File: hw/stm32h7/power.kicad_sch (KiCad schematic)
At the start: 40 parts, among them J5 436500212, U4 LMR50410, U5 INA241A3xDDF, U6 TPS2116DRL, U7 TLV75733PDRV, U8 TLV75733PDRV

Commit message: WIP: H7 dual-axis encoder ports, VSENSE, LED swap, TPS2553/ESD on J4
- driver sheet: respaced; DRV8316C 3x-PWM pinout; J4 encoder port with
  100R series, 2.2k/5.1k pull-ups, TPD4E05U06 ESD array, TPS2553 current
  limited 5V switch (ENC_EN/ENC_SW_nFLT); phase VSENSE dividers
  (100k/8.2k, 8.2p/100p compensated); R55/R58/R62 footprint -> R_0201
- root sheet: second driver instance (driver2) for the dual-axis plan
- micro sheet: D1/D2 -> WS2812B-2020-V6 (3.3V logic), 5V0 feed
- power sheet: drop 3V3_VSENSE_AI (VREFINT instead), LMR50410 cleanup
- stm32h7.ioc: TIM1/TIM8 PWM, SPI2/SPI3/SPI4, TIM4 encoder, FDCAN1/2,
  QUADSPI bank 2
- datasheets: WS2812B-2020-V6, SK6805-EC15, TPS2553
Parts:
- removed C39: 0.1uF, Capacitor_SMD:C_0201_0603Metric, symbol Device:C_Small
- removed R21, R22: 5.1k, Resistor_SMD:R_0201_0603Metric, symbol Device:R_Small
- renumbered C30 to C32, C31 to C33, C32 to C34, C33 to C35, C34 to C36, C35 to C37, C36 to C38, C37 to C39, C38 to C40, C40 to C42, C41 to C43, R10 to R18, R11 to R19, R12 to R20, R13 to R21, R14 to R22, R15 to R23, R16 to R24, R17 to R25, R18 to R26, R19 to R27, R20 to R28, TP9 to TP10, TP3 to TP4, TP4 to TP5, TP5 to TP6, TP6 to TP7, TP7 to TP8, TP8 to TP9, U4 to U5, U5 to U6, U6 to U7, U7 to U8, U8 to U9
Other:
- moved on the sheet: D3, R28

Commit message: WIP: schematic bringup
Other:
- moved on the sheet: C32, C34, C36, C37, L1, R18, R19, R22, R23, R24, R25, TP4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

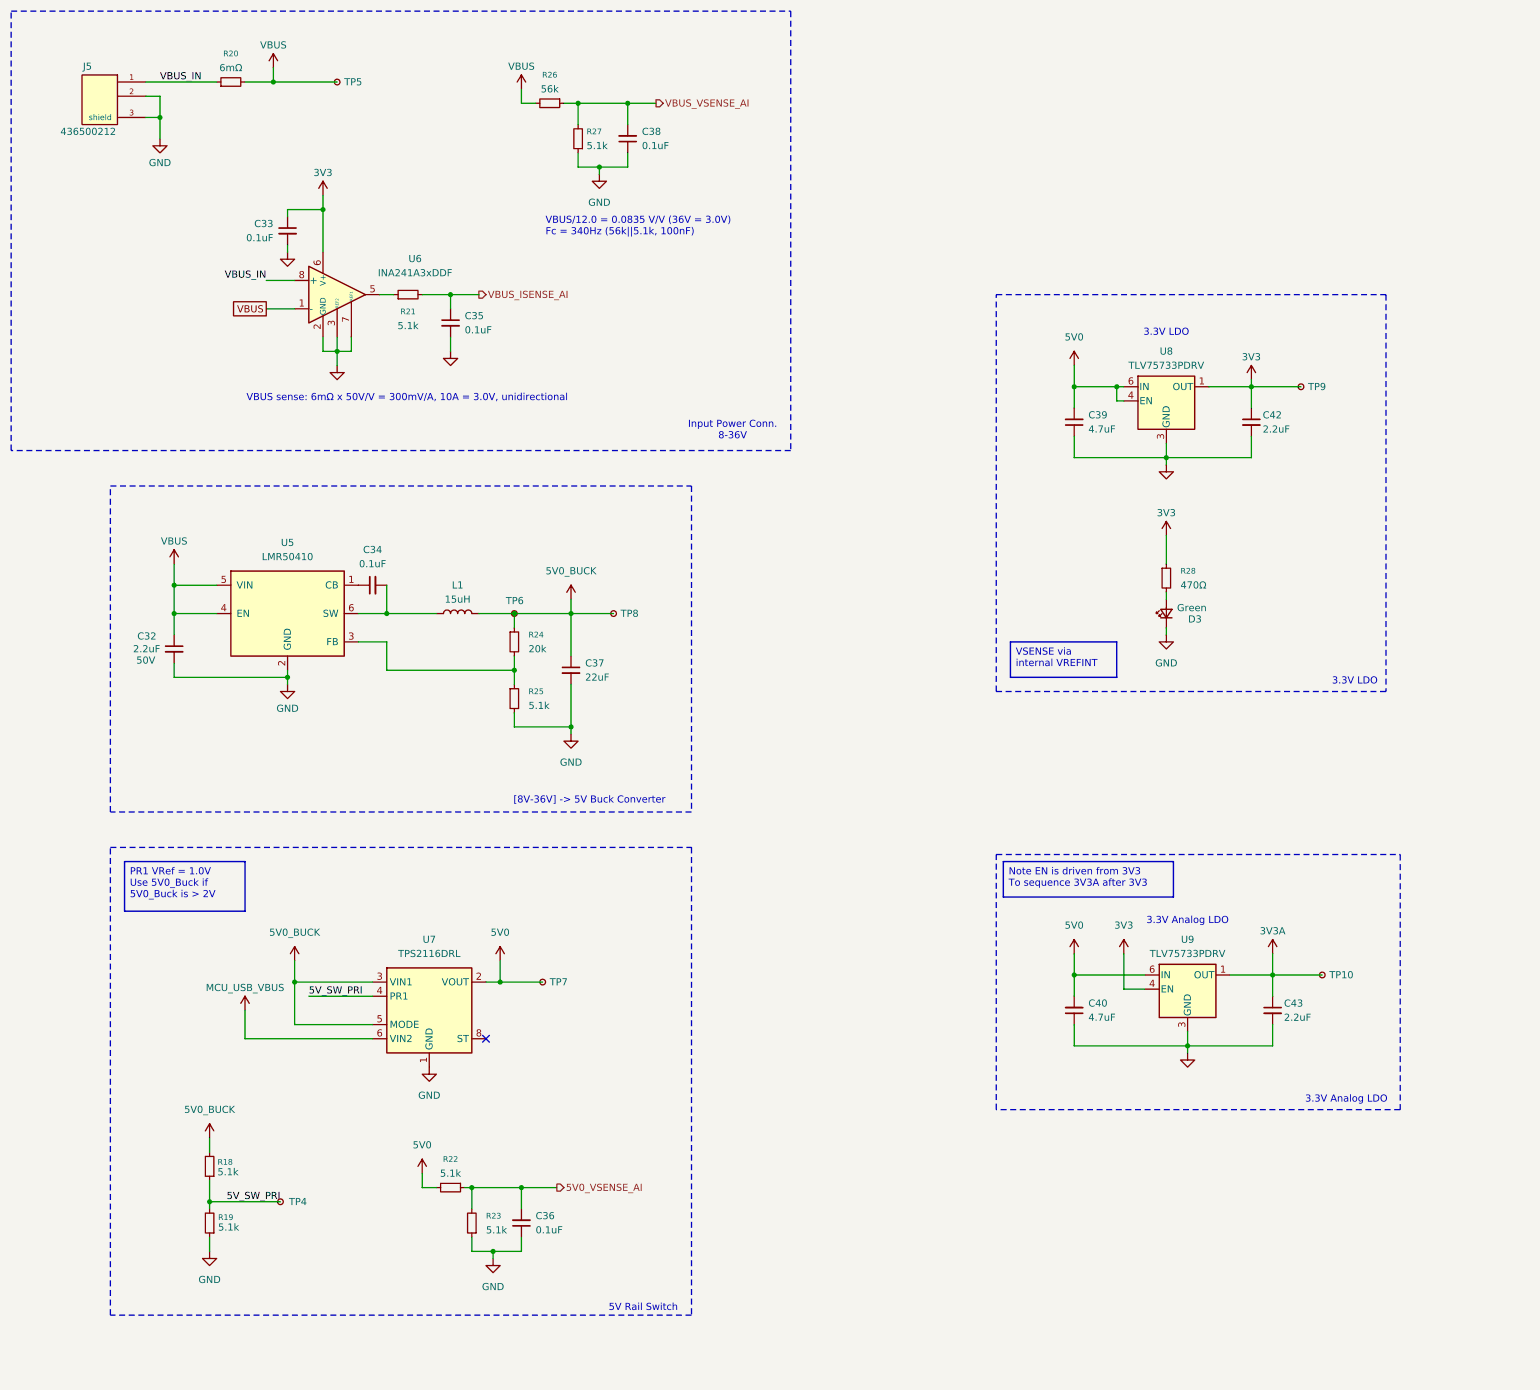
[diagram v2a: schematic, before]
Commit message: WIP: H7 pin plan complete on micro sheet + .ioc, expansion 5V switch
- micro: QSPI bank 2, FDCAN1/2, USB, SPI4 DRV bus + nCS, driver
  nSLEEP/DRVOFF/INLx GPIOs, TIM15_CH1 RGB_DIN, USR_BTN1, LAN9252
  IRQ/SYNC0/SYNC1/nRST, USART3 + RS485 DE, I2C1 to expansion header
- micro: TPS2553 nFAULT wire-OR -> PWR_nFLT (PD11), EXP_PWR_EN on PD0,
  ENC2_SCK moved to PD3
- power: TPS2553 switched 5V0_EXP rail for the expansion header (~1A)
- .ioc: matching assignments, TIM15 and USART3/I2C1 added, PB11 dropped
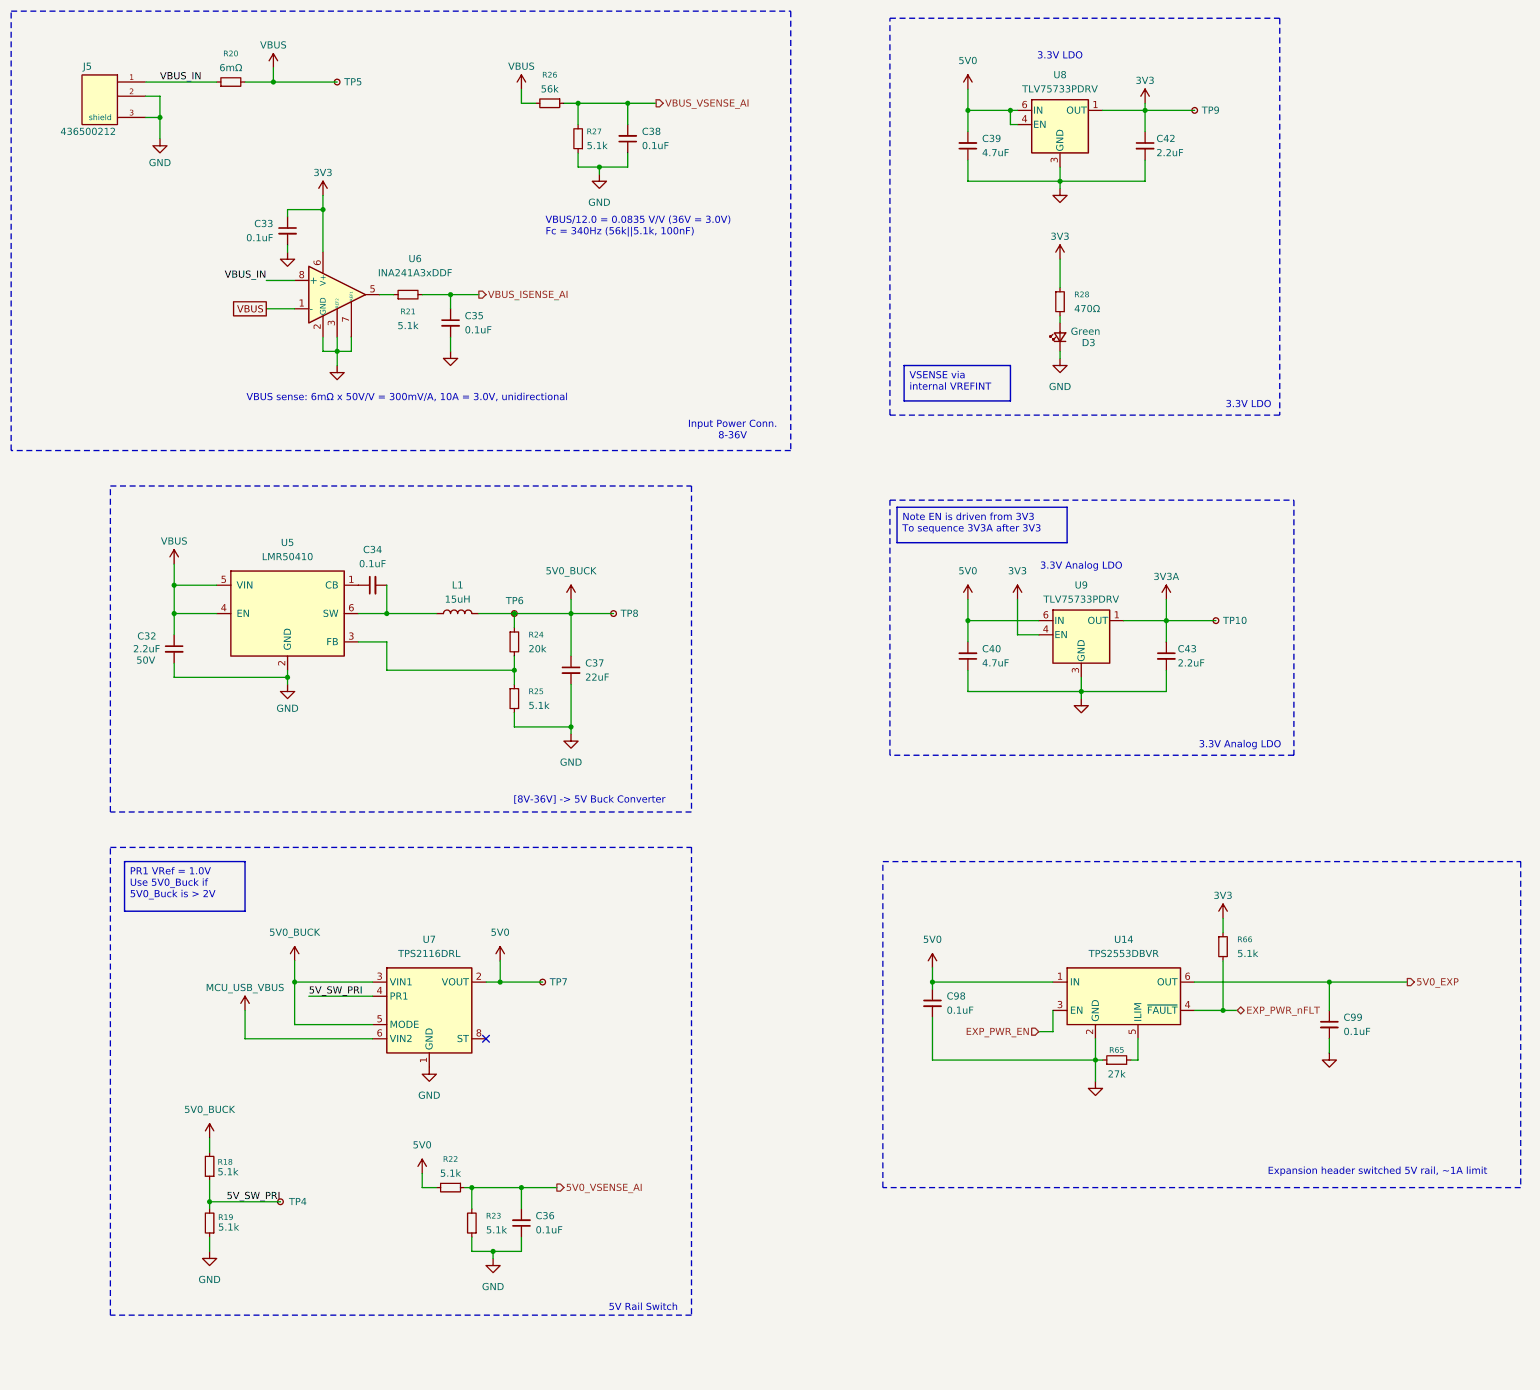
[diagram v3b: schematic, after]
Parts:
- added C98, C99: 0.1uF, Capacitor_SMD:C_0201_0603Metric, symbol Device:C_Small
- added R65: 27k, Resistor_SMD:R_0201_0603Metric, symbol Device:R_Small
- added R66: 5.1k, Resistor_SMD:R_0201_0603Metric, symbol Device:R_Small
- added U14: TPS2553DBVR, pcs_lib:SOT-23-6_TI_DBV0006A, symbol pcs_bldc_sym_lib:TPS2553DBVR
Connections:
- net 3V3: now also R66.1
- net 5V0: now also C98.1, U14.1 (IN)
- net GND: now also C98.2, C99.2, R65.1, U14.2 (GND)
- new net: R65.2, U14.5 (ILIM)
- new net 5V0_EXP: C99.1, U14.6 (OUT)
- new net EXP_PWR_EN: U14.3 (EN)
- new net EXP_PWR_nFLT: R66.2, U14.4 (~{FAULT})
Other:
- note added: "Expansion header switched 5V rail, ~1A limit"
- moved on the sheet: C39, C40, C42, C43, D3, R28, TP10, TP9, U8, U9

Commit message: WIP: H7 schematic and PCB layout progress
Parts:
- removed J5: 436500212, pcs_lib:CONN_SD-43650-005_02_MOL, symbol pcs_bldc_sym_lib:436500212
- renumbered C32 to C46, C33 to C47, C34 to C48, C35 to C49, C36 to C50, C37 to C51, C38 to C52, C98 to C53, C39 to C54, C40 to C55, C42 to C56, C43 to C57, C99 to C58, D3 to D7, R18 to R29, R19 to R30, R20 to R31, R21 to R32, R22 to R33, R23 to R34, R24 to R35, R25 to R36, R26 to R37, R27 to R38, R28 to R39, R65 to R40, R66 to R41, TP4 to TP3, TP5 to TP4, TP6 to TP5, TP7 to TP6, TP8 to TP7, TP9 to TP8, TP10 to TP9, U9 to U10, U14 to U11, U5 to U6, U6 to U7, U7 to U8, U8 to U9
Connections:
- net 5V0_EXP renamed EXP_5V0_SW
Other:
- moved on the sheet: R31, TP4
